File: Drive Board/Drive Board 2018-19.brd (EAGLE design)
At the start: 379.8 x 115 mm, 77 parts, among them IC1 ACS758KCB, IC2 ACS758KCB, IC3 ACS758KCB, IC4 ACS758KCB, IC5 7812T, IC6 LM741P, K1 G5L, K2 G5L, K3 G5L

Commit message: Fixed Battery terminal pad connection
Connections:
- net BATTERY_V+: now also U$7.LEFTHOLE, U$7.P$2, U$7.RIGHTHOLE
- net GND: now also U$9.LEFTHOLE, U$9.P$2, U$9.RIGHTHOLE

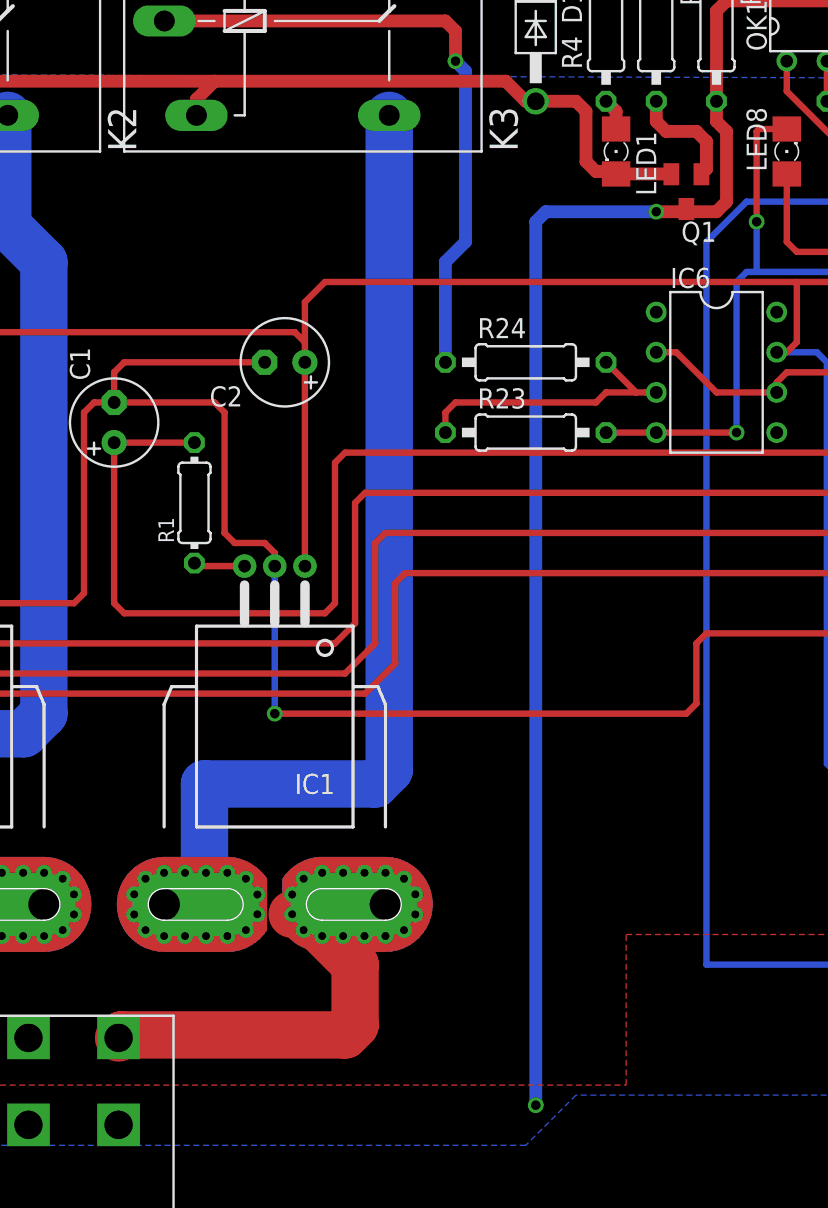
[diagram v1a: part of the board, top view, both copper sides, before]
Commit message: Fixed overlap of trace for current sensor
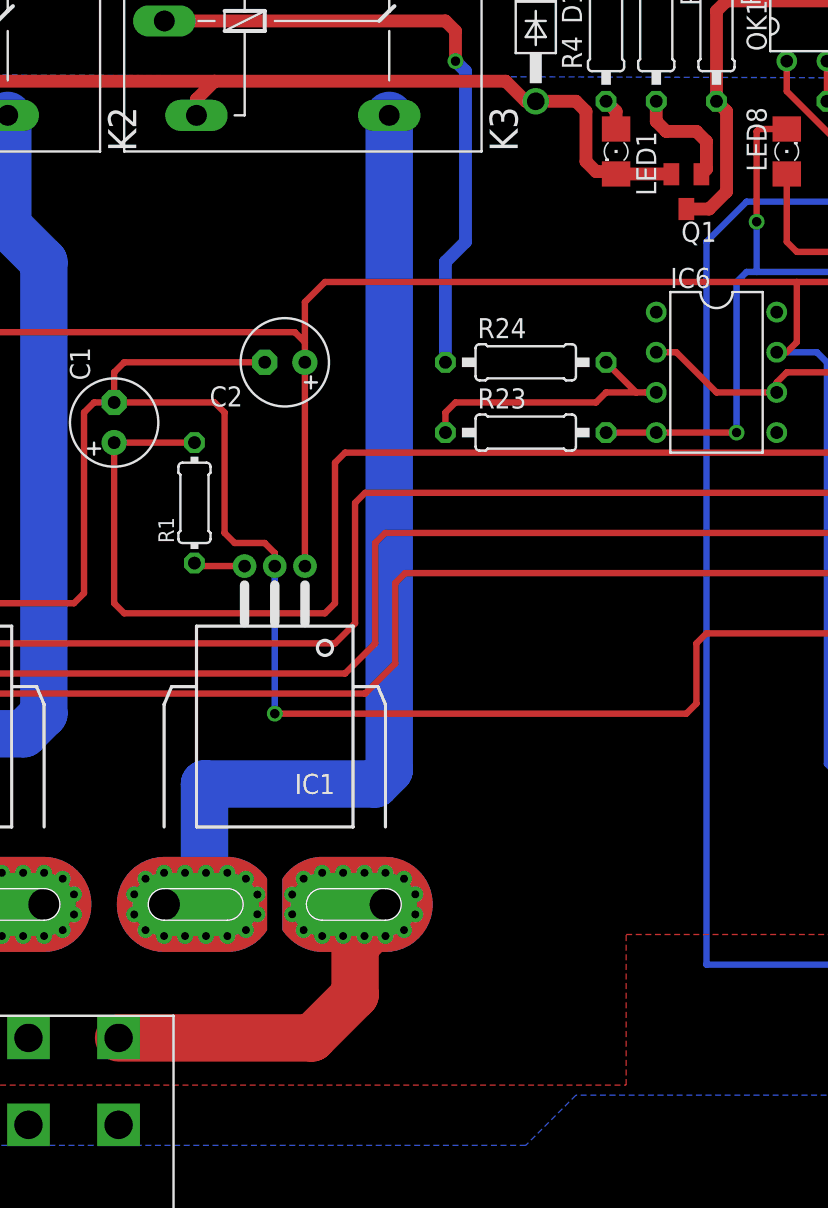
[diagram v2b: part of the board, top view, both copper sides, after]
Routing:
- net BATTERY_V-: track 122.1 -> 55.7 mm, vias 2 -> 0
- net OUT1: track 24.4 -> 20.1 mm

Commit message: fixed mixed ground network
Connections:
- removed net BATTERY_V-: C7.2, C8.2, IC5.2, Q1.3, R7.2
- net GND: now also C7.2, C8.2, IC5.2, Q1.3, R7.2
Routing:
- net GND: track 734.9 -> 827.7 mm
- net BATTERY_V-: track 55.7 -> 0.00 mm
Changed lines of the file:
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@@
 <wire x1="195.66" y1="92.67" x2="196.86" y2="94.78" width="0" layer="19" extent="1-1"/>
-</signal>
-<signal name="BATTERY_V-">
-<contactref element="Q1" pad="3"/>
-<contactref element="R7" pad="2"/>
-<contactref element="IC5" pad="2"/>
-<contactref element="C7" pad="2"/>
-<contactref element="C8" pad="2"/>
-<wire x1="159.385" y1="90.805" x2="156.845" y2="90.805" width="0.8128" layer="1"/>
-<wire x1="156.845" y1="90.805" x2="156.845" y2="87.63" width="0.8128" layer="1"/>
-<wire x1="156.845" y1="87.63" x2="156.21" y2="86.995" width="0.8128" layer="1"/>
-<wire x1="156.21" y1="86.995" x2="140.97" y2="86.995" width="0.8128" layer="1"/>
-<wire x1="140.97" y1="86.995" x2="140.335" y2="86.36" width="0.8128" layer="1"/>
-<wire x1="140.335" y1="86.36" x2="140.335" y2="80.645" width="0.8128" layer="1"/>
-<wire x1="159.385" y1="90.805" x2="159.385" y2="98.425" width="0.8128" layer="1"/>
-<wire x1="159.385" y1="98.425" x2="160.02" y2="99.06" width="0.8128" layer="1"/>
-<wire x1="160.02" y1="99.06" x2="166.37" y2="99.06" width="0.8128" layer="1"/>
-<wire x1="166.37" y1="99.06" x2="167.005" y2="98.425" width="0.8128" layer="1"/>
-<wire x1="167.005" y1="95.885" x2="167.005" y2="98.425" width="0.8128" layer="1"/>
-<wire x1="138.43" y1="73.83" x2="139.87" y2="73.83" width="0.8128" layer="1"/>
-<wire x1="139.87" y1="73.83" x2="140.97" y2="74.93" width="0.8128" layer="1"/>
-<wire x1="140.97" y1="74.93" x2="140.97" y2="80.01" width="0.8128" layer="1"/>
-<wire x1="140.97" y1="80.01" x2="140.335" y2="80.645" width="0.8128" layer="1"/>
 </signal>
 <signal name="OUTA1">
@@
 <contactref element="U$9" pad="P$2" route="any" routetag="G$1.CONTACT"/>
 <contactref element="U$9" pad="RIGHTHOLE" route="any" routetag="G$1.CONTACT"/>
+<contactref element="IC5" pad="2"/>
+<contactref element="C7" pad="2"/>
+<contactref element="C8" pad="2"/>
+<wire x1="159.385" y1="90.805" x2="156.845" y2="90.805" width="0.8128" layer="1"/>
+<wire x1="159.385" y1="90.805" x2="159.385" y2="98.425" width="0.8128" layer="1"/>
+<wire x1="159.385" y1="98.425" x2="160.02" y2="99.06" width="0.8128" layer="1"/>
+<wire x1="160.02" y1="99.06" x2="166.37" y2="99.06" width="0.8128" layer="1"/>
+<wire x1="166.37" y1="99.06" x2="167.005" y2="98.425" width="0.8128" layer="1"/>
+<wire x1="167.005" y1="95.885" x2="167.005" y2="98.425" width="0.8128" layer="1"/>
+<contactref element="Q1" pad="3"/>
+<contactref element="R7" pad="2"/>
+<wire x1="156.845" y1="87.63" x2="156.21" y2="86.995" width="0.8128" layer="1"/>
+<wire x1="156.21" y1="86.995" x2="140.97" y2="86.995" width="0.8128" layer="1"/>
+<wire x1="140.97" y1="86.995" x2="140.335" y2="86.36" width="0.8128" layer="1"/>
+<wire x1="140.335" y1="86.36" x2="140.335" y2="80.645" width="0.8128" layer="1"/>
+<wire x1="139.87" y1="73.83" x2="140.97" y2="74.93" width="0.8128" layer="1"/>
+<wire x1="140.97" y1="74.93" x2="140.97" y2="80.01" width="0.8128" layer="1"/>
+<wire x1="140.97" y1="80.01" x2="140.335" y2="80.645" width="0.8128" layer="1"/>
+<wire x1="112.395" y1="41.91" x2="112.395" y2="40.64" width="0.4064" layer="1"/>
+<wire x1="112.395" y1="40.64" x2="113.665" y2="39.37" width="0.4064" layer="1"/>
+<wire x1="113.665" y1="39.37" x2="134.62" y2="39.37" width="0.4064" layer="1"/>
+<wire x1="134.62" y1="39.37" x2="135.255" y2="38.735" width="0.4064" layer="1"/>
+<wire x1="135.255" y1="38.735" x2="135.255" y2="26.67" width="0.4064" layer="1"/>
+<wire x1="139.87" y1="73.83" x2="138.43" y2="73.83" width="0.8128" layer="1"/>
+<wire x1="142.875" y1="78.74" x2="142.24" y2="78.74" width="0.8128" layer="1"/>
+<wire x1="142.24" y1="78.74" x2="140.335" y2="80.645" width="0.8128" layer="1"/>
+<wire x1="156.845" y1="87.63" x2="156.845" y2="90.805" width="0" layer="19" extent="1-1"/>
 </signal>
 <signal name="A5">

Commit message: Added Components for relay
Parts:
- removed U$8: JTN1AS-PA-F-DC12V, RSX_driver_relay:JTN1AS-PA-F-DC12V
- added D2, D3, D4: 1N4004, diode:DO41-10
- added LED10, LED11, LED12, LED13, LED14, LED9: (no value), eagle-ltspice:LED_1206
- added OK2, OK3, OK4: SFH618A-2, optocoupler:DIP4
- added Q2, Q3, Q4: (no value), semicon-smd-ipc:SOT23
- added R27, R33, R39: 470, resistor:0207/10
- added R28, R29, R34, R35, R40, R41: 4.7k, resistor:0207/10
- added R30, R36, R42: 330, resistor:0207/10
- added R31, R37, R43: 100k, resistor:0207/10
- added R32, R38, R44: 500, resistor:0207/10
- added S1, S10, S2, S9: (no value), switch-dil:DS-01
- moved OK1 183.7 mm to (-35.6, 59.7)
- moved R4 179.3 mm to (-43.8, 58.4)
- moved Q1 179.2 mm to (-40.6, 67.3)
- moved D1 178.9 mm to (-47.6, 56.5)
- moved R25 177.0 mm to (-17.1, 56.5)
- moved LED1 173.9 mm to (-38.1, 52.7)
- moved R26 173.7 mm to (-14.6, 62.9)
- moved R7 170.4 mm to (-28.6, 62.9)
- moved LED8 168.2 mm to (-21.6, 52.7)
- moved R8 167.4 mm to (-14.6, 69.2)
- moved R6 160.7 mm to (-22.2, 61.0)
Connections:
- removed net COIL_V+: B2.VIN, C8.1, D1.C, IC5.3, K1.2, K2.2, K3.2, OK1.4, R4.2, U$11.COI_V_+, U$8.COI_V_+
- removed net COIL_V-: D1.A, K1.1, K2.1, K3.1, LED1.C, Q1.2, U$11.COIL_V_-, U$8.COIL_V_-
- new net COIL_V-_1: D1.A, LED1.C, Q1.2, U$11.COIL_V_-
- new net COIL_V-_2: D2.A, K3.1, LED9.C, Q2.2
- new net COIL_V-_3: D3.A, K2.1, LED11.C, Q3.2
- new net COIL_V-_4: D4.A, K1.1, LED13.C, Q4.2
- new net N$11: OK2.3, R28.1, R29.1
- new net N$12: OK2.2, R30.2
- new net N$14: LED10.A, R32.1
- new net N$15: LED11.A, R33.1
- new net N$18: Q3.1, R34.2
- new net N$20: OK3.3, R34.1, R35.1
- new net N$22: OK3.2, R36.2
- new net N$23: LED12.A, R38.1
- new net N$25: LED13.A, R39.1
- new net N$26: Q4.1, R40.2
- new net N$27: OK4.3, R40.1, R41.1
- new net N$28: OK4.2, R42.2
- new net N$29: LED14.A, R44.1
- new net N$7: LED9.A, R27.1
- new net N$9: Q2.1, R28.2
- new net OPTO1: OK2.1, R31.1, R32.2, S9.1
- new net OPTO2: OK3.1, R37.1, R38.2, S2.1
- new net OPTO3: OK4.1, R43.1, R44.2, S1.1
- new net OPTO4: OK1.1, R25.1, R26.2, S10.1
- new net VOLTAGE_REG_OUT: B2.VIN, C8.1, D1.C, D2.C, D3.C, D4.C, IC5.3, K1.2, K2.2, K3.2, OK1.4, OK2.4, OK3.4, OK4.4, R27.2, R33.2, R39.2, R4.2, U$11.COI_V_+
- net 5V: now also S1.2, S10.2, S2.2, S9.2; no longer R25.2
- net BATTERY_V+: no longer U$8.VIN
- net D12: no longer OK1.1, R25.1, R26.2
- net GND: now also LED10.C, LED12.C, LED14.C, Q2.3, Q3.3, Q4.3, R25.2, R29.2, R30.1, R31.2, R35.2, R36.1, R37.2, R41.2, R42.1, R43.2
- net N$24: no longer U$8.NO
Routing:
- net COIL_V+: track 323.5 -> 0.00 mm
- net VOLTAGE_REG_OUT: track 0.00 -> 206.5 mm
- net COIL_V-: track 197.5 -> 0.00 mm
- net COIL_V-_4: track 0.00 -> 87.9 mm
- net GND: track 827.7 -> 747.4 mm
- net N$1: track 25.1 -> 0.00 mm
- net D12: track 143.2 -> 125.2 mm
- net N$21: track 11.8 -> 0.00 mm
- net N$16: track 7.18 -> 0.00 mm
- net N$34: track 2.54 -> 0.00 mm
- net N$3: track 2.02 -> 0.00 mm
- net 5V: track 265.8 -> 263.9 mm

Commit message: Finished Layout for Relay support circuitry
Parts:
- moved R28 93.0 mm to (127.0, 97.8)
- moved D2 86.4 mm to (127.0, 91.4), turned to 0 degrees
- moved R27 84.3 mm to (127.0, 94.6), turned to 180 degrees
- moved D4 83.6 mm to (57.1, 92.7)
- moved R31 83.3 mm to (115.6, 103.5), turned to 270 degrees
- moved S10 82.8 mm to (17.1, 22.9), turned to 180 degrees
- moved OK2 82.4 mm to (125.7, 104.8), turned to 90 degrees
- moved S1 81.9 mm to (69.8, 105.4)
- moved R29 80.7 mm to (127.0, 101.0)
- moved Q4 79.1 mm to (70.5, 95.9), turned to 270 degrees
- moved Q2 78.4 mm to (141.0, 93.3), turned to 270 degrees
- moved D1 75.5 mm to (25.4, 37.5), turned to 180 degrees
- moved D3 75.1 mm to (93.3, 92.1)
- moved R4 73.1 mm to (25.4, 34.9), turned to 0 degrees
- moved R30 72.9 mm to (118.1, 103.5), turned to 90 degrees
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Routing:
- net 5V: track 263.9 -> 571.5 mm, vias 0 -> 1
- net GND: track 747.4 -> 1048.7 mm
- net VOLTAGE_REG_OUT: track 206.5 -> 401.2 mm
- net D12: track 125.2 -> 0.00 mm
- net COIL_V-_2: track 0.00 -> 49.9 mm
- net COIL_V-_4: track 87.9 -> 38.0 mm
- net OPTO2: track 0.00 -> 46.0 mm
- net OPTO3: track 0.00 -> 44.2 mm
- net OPTO1: track 0.00 -> 43.0 mm
- net COIL_V-_3: track 0.00 -> 40.8 mm
- net COIL_V-_1: track 0.00 -> 24.9 mm
- net OPTO4: track 0.00 -> 15.5 mm
- net N$12: track 0.00 -> 15.2 mm
- net N$22: track 0.00 -> 15.1 mm
- net N$28: track 0.00 -> 15.1 mm
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
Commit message: Relay control from DIO pins implemented
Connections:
- new net A4: B2.A4, IC6.2, IC6.6
- net 5V: no longer S1.2, S2.2, S9.2
- net A5: now also S9.2; no longer IC6.2, IC6.6
- net D12: now also S1.2
- net D13: now also S2.2
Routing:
- net D12: track 0.00 -> 249.9 mm, vias 0 -> 1
- net D13: track 0.00 -> 215.6 mm, vias 0 -> 1
- net 5V: track 571.5 -> 407.3 mm
- net A5: track 17.8 -> 182.0 mm, vias 0 -> 1
- net GND: track 1048.7 -> 896.3 mm, vias 5 -> 2
- net VOLTAGE_REG_OUT: track 401.2 -> 440.9 mm
- net BATTERY_V+: track 34.7 -> 14.2 mm, vias 1 -> 0
- net A4: track 0.00 -> 17.5 mm
- net IC2_IN: track 52.2 -> 55.2 mm
- net 3V3: track 263.6 -> 260.6 mm
- net COIL_V-_2: track 49.9 -> 49.1 mm
- net COIL_V-_3: track 40.8 -> 41.5 mm

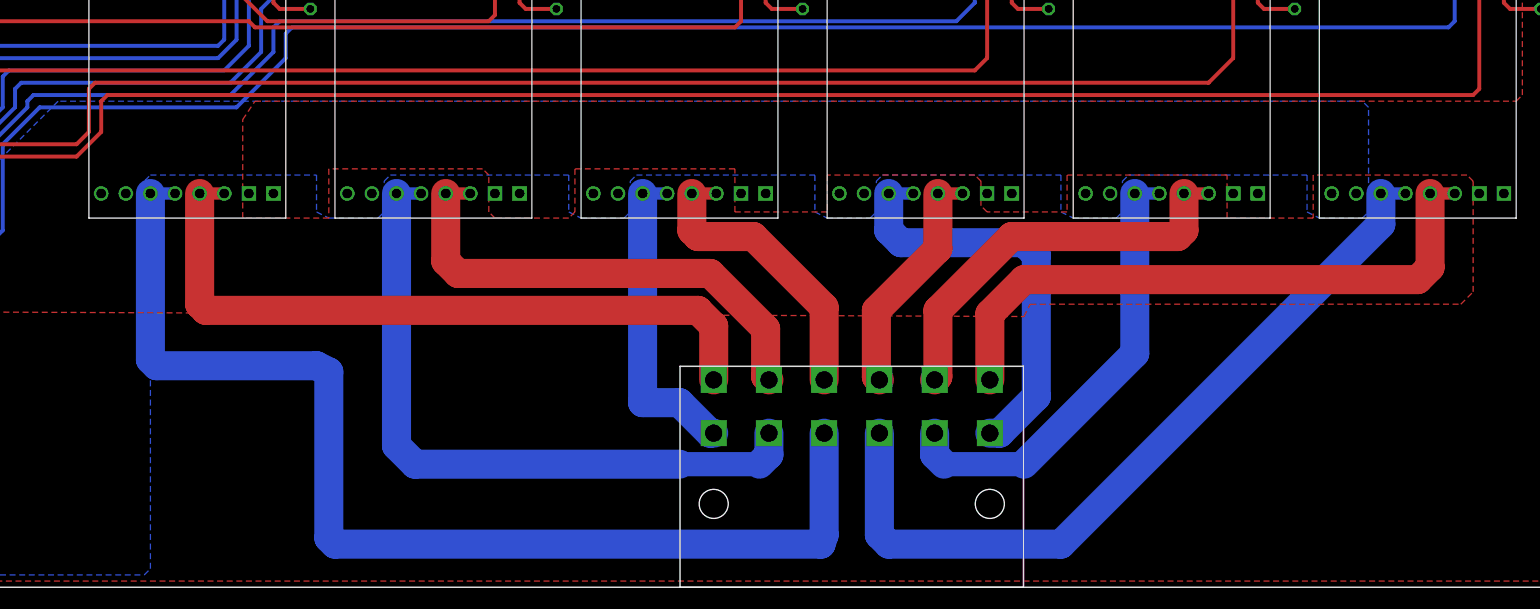
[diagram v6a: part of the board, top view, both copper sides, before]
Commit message: Updated trace width and added connector information
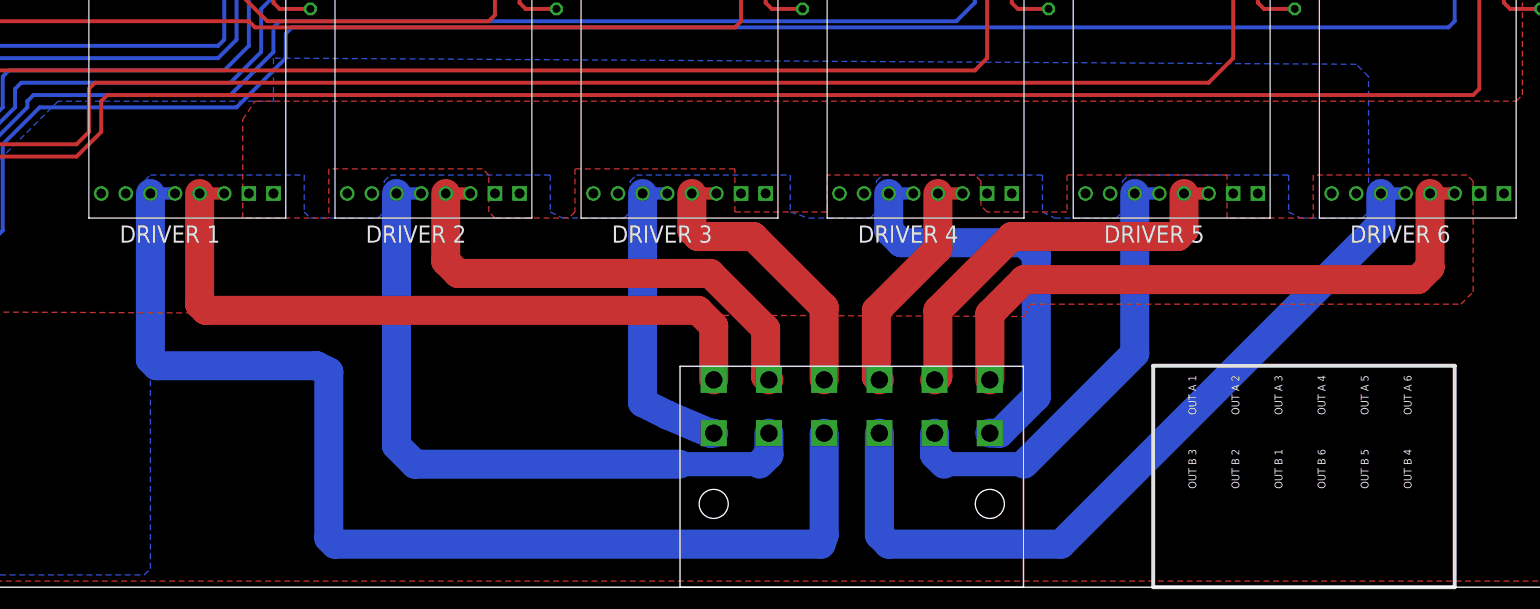
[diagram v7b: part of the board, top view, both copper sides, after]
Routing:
- net OUTA3: track 32.8 -> 32.2 mm
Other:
- board text added: "DRIVER 1"
- board text added: "DRIVER 2"
- board text added: "DRIVER 3"
- board text added: "DRIVER 4"
- board text added: "DRIVER 5"
- board text added: "DRIVER 6"
- board text added: "OUT A 1"
- board text added: "OUT A 2"
- board text added: "OUT A 3"
- board text added: "OUT A 4"
- board text added: "OUT A 5"
- board text added: "OUT A 6"
- board text added: "OUT B 1"
- board text added: "OUT B 2"
- board text added: "OUT B 3"
- board text added: "OUT B 4"
- board text added: "OUT B 5"
- board text added: "OUT B 6"
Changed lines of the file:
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@@
 <hole x="369.8" y="85" drill="3"/>
 <hole x="369.8" y="35" drill="3"/>
+<text x="217.17" y="35.56" size="1.778" layer="25">DRIVER 1</text>
+<text x="242.57" y="35.56" size="1.778" layer="25">DRIVER 2</text>
+<text x="267.97" y="35.56" size="1.778" layer="25">DRIVER 3</text>
+<text x="293.37" y="35.56" size="1.778" layer="25">DRIVER 4</text>
+<text x="318.77" y="35.56" size="1.778" layer="25">DRIVER 5</text>
+<text x="344.17" y="35.56" size="1.778" layer="25">DRIVER 6</text>
+<wire x1="323.85" y1="22.86" x2="354.965" y2="22.86" width="0.4064" layer="25"/>
+<wire x1="354.965" y1="22.86" x2="354.965" y2="0" width="0.4064" layer="25"/>
+<wire x1="354.965" y1="0" x2="323.85" y2="0" width="0.4064" layer="25"/>
+<wire x1="323.85" y1="0" x2="323.85" y2="22.86" width="0.4064" layer="25"/>
+<text x="328.295" y="17.78" size="0.8128" layer="25" rot="R90">OUT A 1</text>
+<text x="332.74" y="17.78" size="0.8128" layer="25" rot="R90">OUT A 2</text>
+<text x="337.185" y="17.78" size="0.8128" layer="25" rot="R90">OUT A 3</text>
+<text x="341.63" y="17.78" size="0.8128" layer="25" rot="R90">OUT A 4</text>
+<text x="346.075" y="17.78" size="0.8128" layer="25" rot="R90">OUT A 5</text>
+<text x="350.52" y="17.78" size="0.8128" layer="25" rot="R90">OUT A 6</text>
+<text x="328.295" y="10.16" size="0.8128" layer="25" rot="R90">OUT B 3</text>
+<text x="332.74" y="10.16" size="0.8128" layer="25" rot="R90">OUT B 2</text>
+<text x="337.185" y="10.16" size="0.8128" layer="25" rot="R90">OUT B 1</text>
+<text x="341.63" y="10.16" size="0.8128" layer="25" rot="R90">OUT B 6</text>
+<text x="346.075" y="10.16" size="0.8128" layer="25" rot="R90">OUT B 5</text>
+<text x="350.52" y="10.16" size="0.8128" layer="25" rot="R90">OUT B 4</text>
 </plain>
 <attributes>
@@
 <vertex x="219.075" y="41.275"/>
 <vertex x="220.345" y="42.545"/>
-<vertex x="237.49" y="42.545"/>
-<vertex x="237.49" y="38.735"/>
-<vertex x="238.76" y="38.1"/>
+<vertex x="236.22" y="42.545"/>
+<vertex x="236.22" y="38.735"/>
+<vertex x="236.855" y="38.1"/>
 <vertex x="243.84" y="38.1"/>
 <vertex x="244.475" y="38.735"/>
 <vertex x="244.475" y="41.91"/>
 <vertex x="245.11" y="42.545"/>
-<vertex x="263.525" y="42.545"/>
-<vertex x="263.525" y="38.735"/>
-<vertex x="264.795" y="38.1"/>
+<vertex x="261.62" y="42.545"/>
+<vertex x="261.62" y="38.735"/>
+<vertex x="262.89" y="38.1"/>
 <vertex x="269.24" y="38.1"/>
 <vertex x="269.875" y="38.735"/>
 <vertex x="269.875" y="41.91"/>
 <vertex x="270.51" y="42.545"/>
-<vertex x="288.925" y="42.545"/>
-<vertex x="288.925" y="38.735"/>
-<vertex x="290.195" y="38.1"/>
+<vertex x="286.385" y="42.545"/>
+<vertex x="286.385" y="38.735"/>
+<vertex x="288.29" y="38.1"/>
 <vertex x="294.64" y="38.1"/>
 <vertex x="295.275" y="38.735"/>
 <vertex x="295.275" y="41.91"/>
 <vertex x="295.91" y="42.545"/>
-<vertex x="314.325" y="42.545"/>
-<vertex x="314.325" y="38.735"/>
-<vertex x="315.595" y="38.1"/>
+<vertex x="312.42" y="42.545"/>
+<vertex x="312.42" y="38.735"/>
+<vertex x="313.69" y="38.1"/>
 <vertex x="320.04" y="38.1"/>
 <vertex x="320.675" y="38.735"/>
 <vertex x="320.675" y="41.91"/>
 <vertex x="321.31" y="42.545"/>
-<vertex x="339.725" y="42.545"/>
-<vertex x="339.725" y="38.735"/>
-<vertex x="340.995" y="38.1"/>
+<vertex x="337.82" y="42.545"/>
+<vertex x="337.82" y="38.735"/>
+<vertex x="339.09" y="38.1"/>
 <vertex x="345.44" y="38.1"/>
 <vertex x="346.075" y="38.735"/>
-<vertex x="346.075" y="49.53"/>
-<vertex x="345.44" y="50.165"/>
+<vertex x="346.075" y="52.705"/>
+<vertex x="344.805" y="53.975"/>
+<vertex x="233.045" y="54.61"/>
+<vertex x="233.045" y="50.165"/>
 <vertex x="210.82" y="50.165"/>
 <vertex x="203.2" y="42.545"/>
@@
 <contactref element="U$12" pad="P$1"/>
 <wire x1="278.485" y1="15.9" x2="278.105" y2="15.9" width="3" layer="16"/>
-<wire x1="278.105" y1="15.9" x2="274.955" y2="19.05" width="3" layer="16"/>
-<wire x1="274.955" y1="19.05" x2="271.145" y2="19.05" width="3" layer="16"/>
+<wire x1="278.105" y1="15.9" x2="273.685" y2="17.78" width="3" layer="16"/>
+<wire x1="273.685" y1="17.78" x2="271.145" y2="19.05" width="3" layer="16"/>
 <wire x1="271.145" y1="19.05" x2="271.145" y2="40.64" width="3" layer="16"/>
 <wire x1="273.685" y1="40.64" x2="271.145" y2="40.64" width="1.27" layer="16"/>
